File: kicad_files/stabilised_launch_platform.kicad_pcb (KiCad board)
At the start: 2 copper layers, 20 parts, among them J1 Conn_01x03_Male, J2 Conn_01x03_Male, J3 Conn_01x04_Male, SW1 SW_Push, U1 MAX7375AXR805, U2 AP7370-33Y, U3 STM32L011F3Px

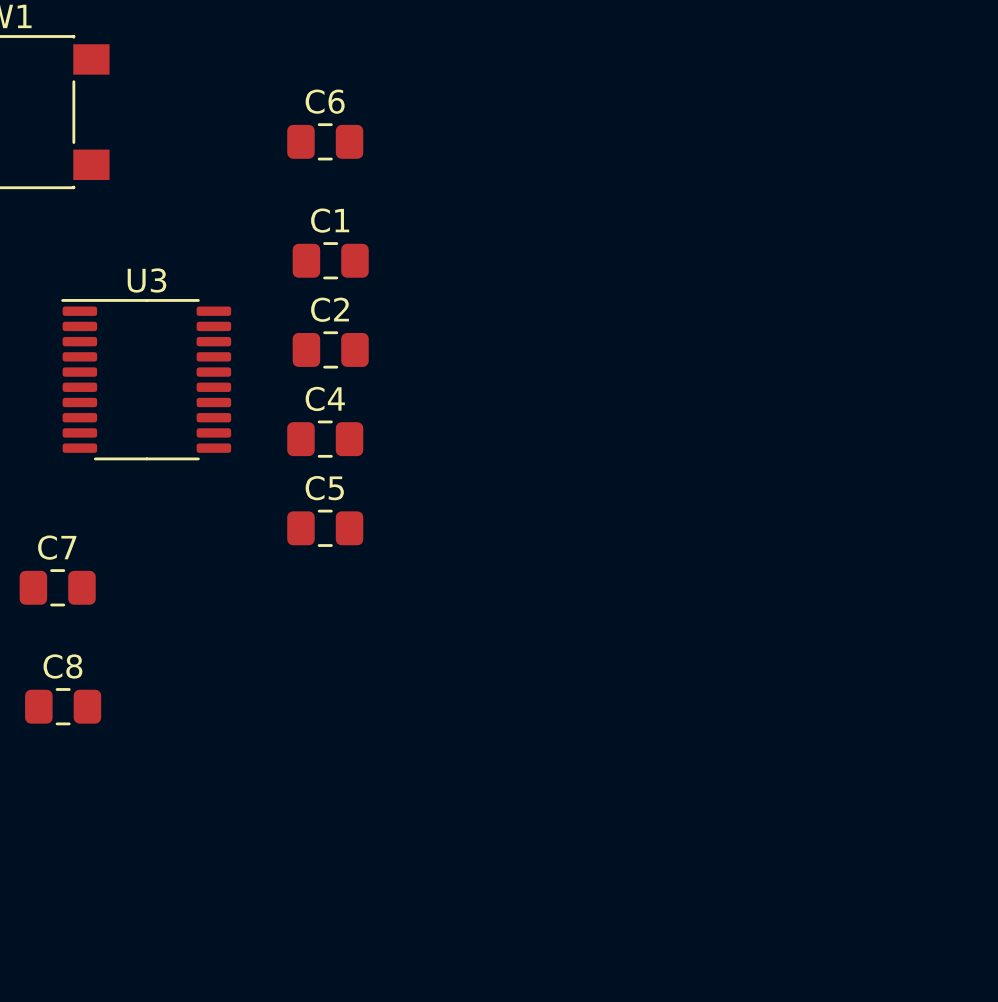
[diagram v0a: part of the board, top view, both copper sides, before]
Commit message: Added accelerometer and MOSFETs to schematic and PCB
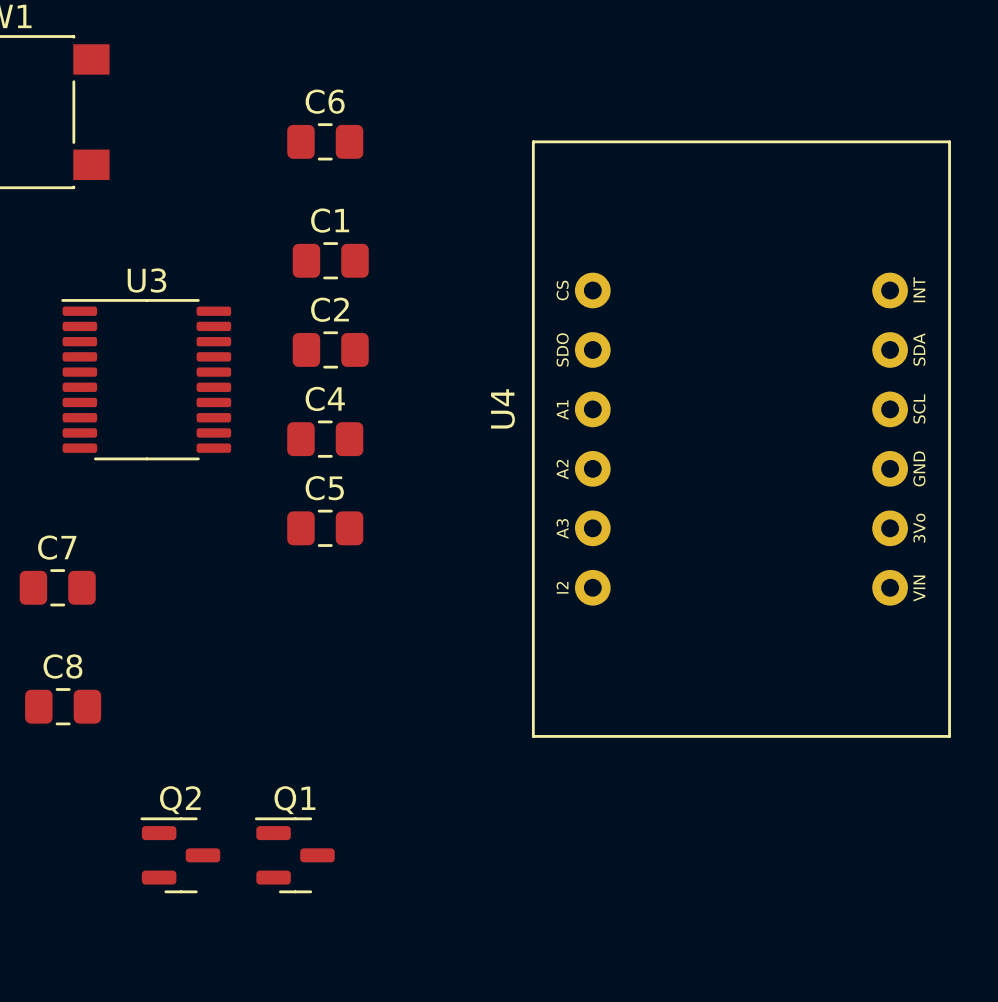
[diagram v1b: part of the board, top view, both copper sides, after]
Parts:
- added Q1: AO3400A, Package_TO_SOT_SMD:SOT-23, F.Cu at (133.3, 101.6)
- added Q2: AO3400A, Package_TO_SOT_SMD:SOT-23, F.Cu at (128.5, 101.6)
- added U4: LIS3DH, CustomFootprints:LIS3DH Accelerometer, F.Cu at (152.4, 83.8)
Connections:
- C7 pad 1: +5V -> SERVO2_SIG_AMP
- J1 pad 1: SERVO1_SIG -> SERVO2_SIG_AMP
- J1 pad 2: +5V -> SERVO2_SIG_AMP
- J2 pad 1: SERVO2_SIG -> SERVO2_SIG_AMP
- J2 pad 2: +5V -> SERVO2_SIG_AMP
- J3 pad 1: +5V -> SERVO2_SIG_AMP
- U2 pad 3: +5V -> SERVO2_SIG_AMP
- U3 pad 11: unconnected-(U3-Pad11) -> POT1
- U3 pad 12: unconnected-(U3-Pad12) -> POT2
- U3 pad 13: POT1 -> POT3
- U3 pad 8: unconnected-(U3-Pad8) -> SERVO1_SIG
- U3 pad 9: unconnected-(U3-Pad9) -> SERVO2_SIG

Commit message: Schematic finished
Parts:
- added C10: 47p, Capacitor_SMD:C_0805_2012Metric_Pad1.18x1.45mm_HandSolder, F.Cu at (110.5, 105.7)
- added C11: 10n, Capacitor_SMD:C_0805_2012Metric_Pad1.18x1.45mm_HandSolder, F.Cu at (105.7, 111.8)
- added C12: 0.1u, Capacitor_SMD:C_0805_2012Metric_Pad1.18x1.45mm_HandSolder, F.Cu at (105.7, 105.7)
- added C13: 47p, Capacitor_SMD:C_0805_2012Metric_Pad1.18x1.45mm_HandSolder, F.Cu at (115.3, 108.8)
- added C14: 4.7u, Capacitor_SMD:C_0805_2012Metric_Pad1.18x1.45mm_HandSolder, F.Cu at (145.6, 80.3)
- added C9: 0.1u, Capacitor_SMD:C_0805_2012Metric_Pad1.18x1.45mm_HandSolder, F.Cu at (105.7, 108.8)
- added FB1: FerriteBead, Inductor_SMD:L_0805_2012Metric_Pad1.05x1.20mm_HandSolder, F.Cu at (125.7, 108.0)
- added J4: USB_C_Receptacle_USB2.0, Connector_USB:USB_C_Receptacle_GCT_USB4085, F.Cu at (83.5, 97.8)
- added JP1: SolderJumper, Jumper:SolderJumper-2_P1.3mm_Open_Pad1.0x1.5mm, F.Cu at (135.9, 97.8)
- added R3: 5.1k, Resistor_SMD:R_0805_2012Metric_Pad1.20x1.40mm_HandSolder, F.Cu at (145.5, 83.3)
- added R4: 5.1k, Resistor_SMD:R_0805_2012Metric_Pad1.20x1.40mm_HandSolder, F.Cu at (120.1, 110.3)
- added R5: 2.2k, Resistor_SMD:R_0805_2012Metric_Pad1.20x1.40mm_HandSolder, F.Cu at (172.0, 64.4)
- added R6: 2.2k, Resistor_SMD:R_0805_2012Metric_Pad1.20x1.40mm_HandSolder, F.Cu at (120.1, 107.4)
- added R7: 4.7k, Resistor_SMD:R_0805_2012Metric_Pad1.20x1.40mm_HandSolder, F.Cu at (130.6, 97.7)
- added R8: 4.7k, Resistor_SMD:R_0805_2012Metric_Pad1.20x1.40mm_HandSolder, F.Cu at (150.3, 80.3)
- added U5: LIS3DH, CustomFootprints:LIS3DH Accelerometer, F.Cu at (156.4, 69.3)
- J3: value Conn_01x04_Male -> Conn_01x06_Male; footprint Connector_PinHeader_1.00mm:PinHeader_1x04_P1.00mm_Vertical -> Connector_PinHeader_1.00mm:PinHeader_1x06_P1.00mm_Vertical
- R1, R2: value 2.2k -> 27R
- U4: value LIS3DH -> FT201XS; footprint CustomFootprints:LIS3DH Accelerometer -> Package_SO:SSOP-16_3.9x4.9mm_P0.635mm
- moved J1 76.1 mm to (82.3, 108.9)
- moved J2 56.7 mm to (100.1, 105.6)
- moved J3 49.5 mm to (113.8, 97.7), turned to 0 degrees
- moved Q1 47.6 mm to (86.4, 109.6)
- moved C5 45.7 mm to (172.1, 61.4)
- moved R2 43.3 mm to (125.8, 100.7), turned to 0 degrees
- moved RV2 43.1 mm to (82.9, 64.2), turned to 0 degrees
- moved C1 43.1 mm to (110.5, 111.8)
- moved R1 40.1 mm to (125.8, 103.6), turned to 0 degrees
- moved SW1 37.9 mm to (97.8, 100.1)
- moved U4 36.5 mm to (119.5, 99.6), turned to 0 degrees
- moved C6 36.3 mm to (120.1, 104.4)
- moved U1 36.2 mm to (150.1, 83.6), turned to 0 degrees
- moved C8 36.1 mm to (91.3, 111.8)
- moved C4 34.0 mm to (115.3, 111.8)
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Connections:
- C7 pad 1: SERVO2_SIG_AMP -> +5V
- J1 pad 1: SERVO2_SIG_AMP -> SERVO1_SIG
- J1 pad 2: SERVO2_SIG_AMP -> +5V
- J2 pad 1: SERVO2_SIG_AMP -> SERVO2_SIG
- J2 pad 2: SERVO2_SIG_AMP -> +5V
- J3 pad 1: SERVO2_SIG_AMP -> +5V
- J3 pad 4: GND -> MCU_TX
- Q1 pad 3: SERVO2_SIG_AMP -> SERVO1_SIG_AMP
- R1 pad 1: +3.3V -> USBDM
- R1 pad 2: SCL -> Net-(R1-Pad2)
- R2 pad 1: +3.3V -> USBDP
- R2 pad 2: SDA -> Net-(R2-Pad2)
- U2 pad 3: SERVO2_SIG_AMP -> +5V
- U3 pad 1: unconnected-(U3-Pad1) -> +3.3V
- U3 pad 10: SCL -> SERVO2_SIG
- U3 pad 17: unconnected-(U3-Pad17) -> SCL
- U3 pad 7: unconnected-(U3-Pad7) -> SERVO1_SIG
- U3 pad 8: SERVO1_SIG -> MCU_TX
- U3 pad 9: SERVO2_SIG -> MCU_RX
- U4 pad 10: GND -> FTDI_3V3
- U4 pad 11: unconnected-(U4-Pad11) -> FTDI_3V3
- U4 pad 12: GND -> Net-(JP1-Pad2)
- U4 pad 2: unconnected-(U4-Pad2) -> SCL
- U4 pad 3: unconnected-(U4-Pad3) -> FTDI_3V3
- U4 pad 4: SCL -> SDA
- U4 pad 6: SDA -> unconnected-(U4-Pad6)
- U4 pad 8: unconnected-(U4-Pad8) -> Net-(R2-Pad2)
- U4 pad 9: unconnected-(U4-Pad9) -> Net-(R1-Pad2)

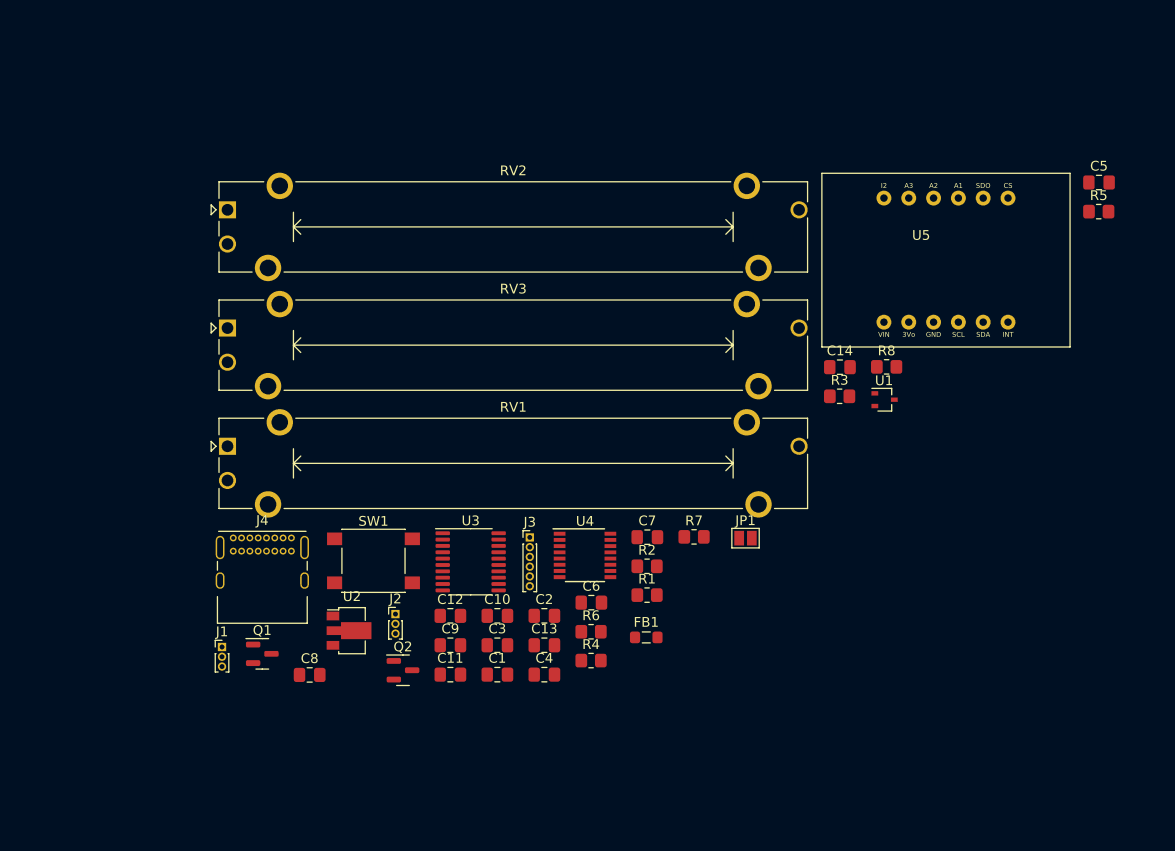
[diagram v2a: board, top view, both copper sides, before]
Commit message: Removed unnecessary mosfets, schematic finished
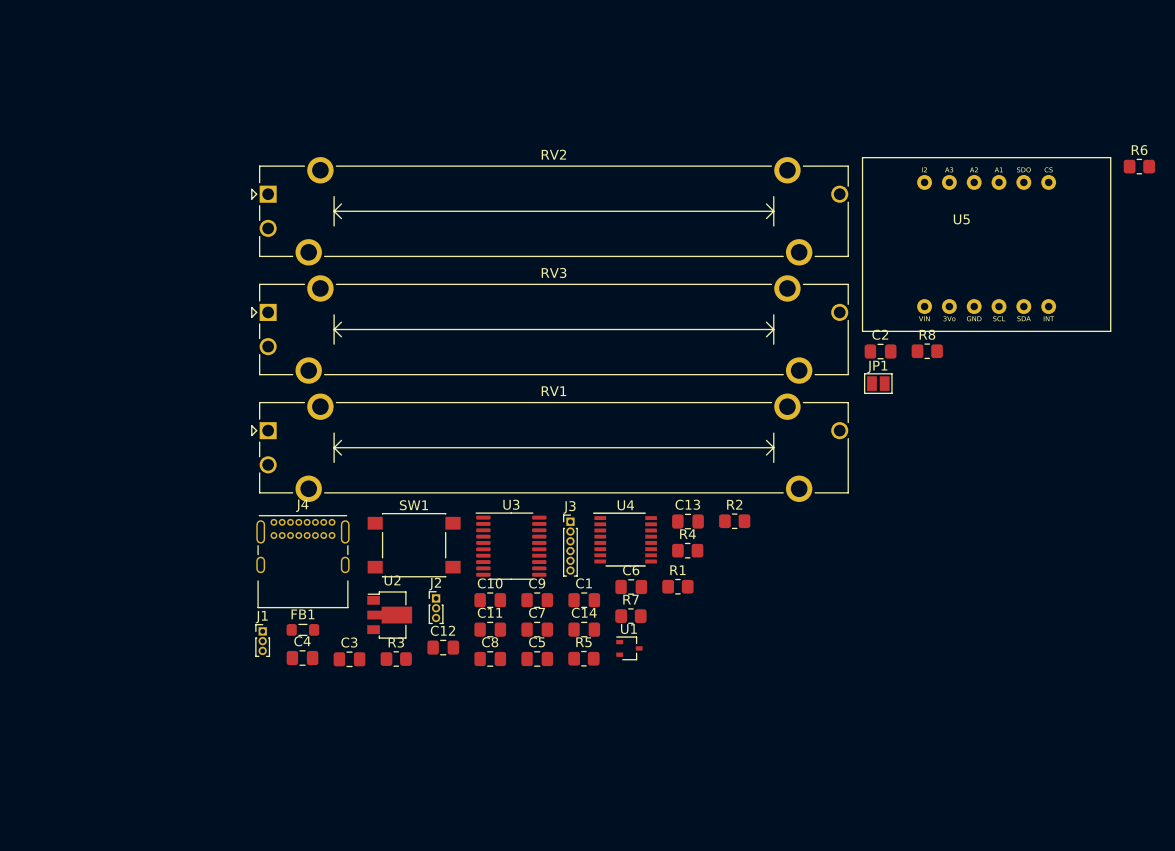
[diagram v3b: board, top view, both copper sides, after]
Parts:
- removed Q1, Q2: AO3400A, Package_TO_SOT_SMD:SOT-23
- moved C5 75.4 mm to (114.6, 110.2)
- moved R6 73.6 mm to (176.2, 59.8)
- moved R5 69.8 mm to (119.3, 110.1)
- moved R3 52.7 mm to (100.1, 110.2)
- moved C2 43.8 mm to (149.7, 78.7)
- moved C14 37.5 mm to (119.4, 107.2)
- moved U1 36.5 mm to (124.0, 109.1)
- moved FB1 35.1 mm to (90.6, 107.2)
- moved C4 24.8 mm to (90.5, 110.1)
- moved JP1 20.9 mm to (149.5, 82.0)
- moved C13 19.4 mm to (130.0, 96.1)
- moved C8 18.6 mm to (109.8, 110.2)
- moved C3 15.2 mm to (95.4, 110.2)
- moved R4 15.0 mm to (130.0, 99.1)
- moved C7 14.7 mm to (114.6, 107.2)
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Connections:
- R7 pad 2: SERVO1_SIG_AMP -> SERVO1_SIG
- R8 pad 2: SERVO2_SIG_AMP -> SERVO2_SIG

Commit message: PCB tracks routed have all components connected, needs a bit of tidying up
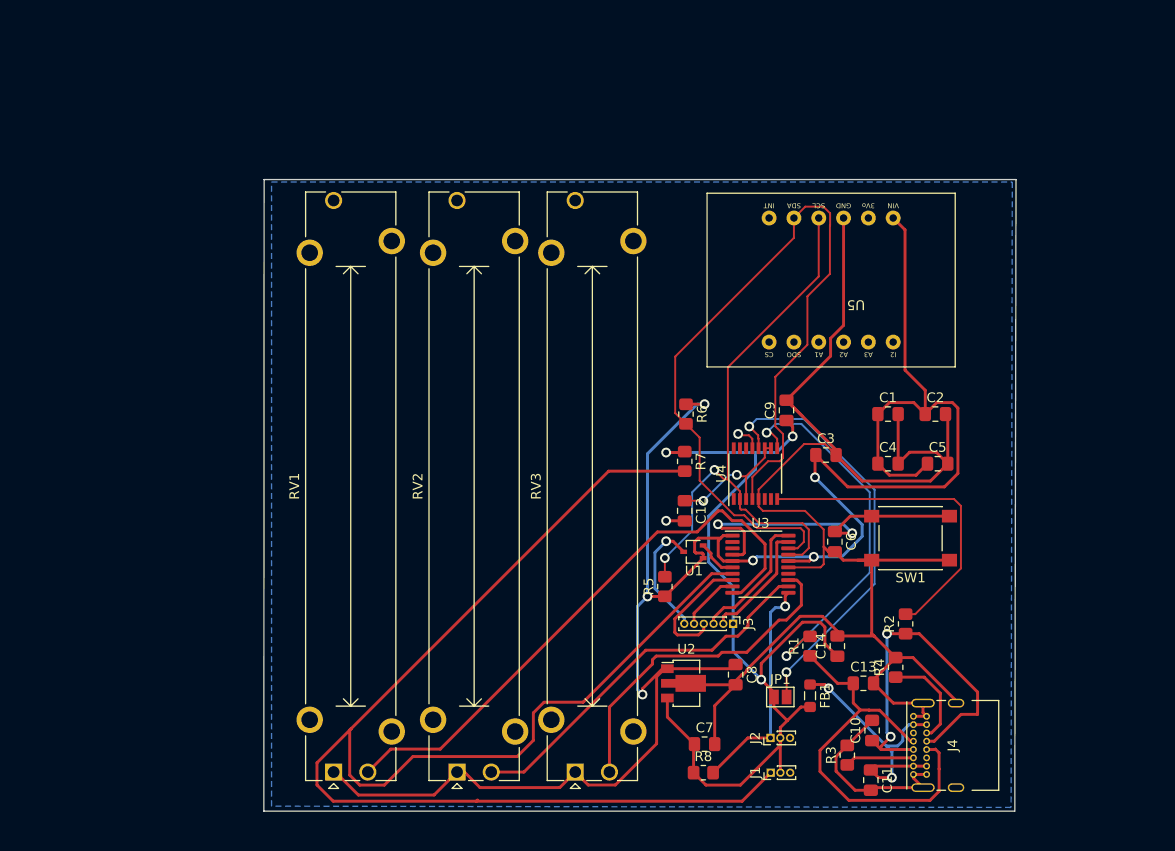
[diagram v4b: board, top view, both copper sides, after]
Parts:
- moved J4 70.4 mm to (153.1, 122.0), turned to 90 degrees
- moved C4 63.1 mm to (150.5, 90.2)
- moved RV2 62.2 mm to (106.4, 121.7), turned to 90 degrees
- moved RV3 56.6 mm to (118.5, 121.7), turned to 90 degrees
- moved J1 54.0 mm to (138.5, 121.8), turned to 90 degrees
- moved C3 53.1 mm to (144.1, 89.3)
- moved R6 52.9 mm to (129.8, 85.1), turned to -90 degrees
- moved FB1 52.3 mm to (142.5, 113.9), turned to -90 degrees
- moved SW1 50.8 mm to (152.8, 97.8), turned to 180 degrees
- moved R8 48.8 mm to (131.6, 121.8)
- moved R3 47.2 mm to (146.3, 120.0), turned to 90 degrees
- moved C5 45.6 mm to (155.6, 90.2)
- moved C11 41.9 mm to (148.7, 122.6), turned to -90 degrees
- moved C10 41.3 mm to (148.8, 117.5), turned to 90 degrees
- moved J2 37.1 mm to (138.4, 118.2), turned to 90 degrees
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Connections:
- U3 pad 10: SERVO2_SIG -> POT1
- U3 pad 11: POT1 -> SERVO2_SIG
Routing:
- net +3.3V: track 0.00 -> 203.7 mm, vias 0 -> 6
- net GND: track 0.00 -> 203.2 mm, vias 0 -> 3
- net SERVO1_SIG: track 0.00 -> 155.8 mm
- net +5V: track 0.00 -> 93.8 mm, vias 0 -> 3
- net SDA: track 0.00 -> 87.0 mm
- net SCL: track 0.00 -> 61.1 mm, vias 0 -> 2
- net POT1: track 0.00 -> 60.0 mm
- net Net-(JP1-Pad2): track 0.00 -> 43.7 mm, vias 0 -> 2
- net USBDM: track 0.00 -> 42.6 mm
- net Net-(R1-Pad2): track 0.00 -> 39.7 mm, vias 0 -> 2
- net POT2: track 0.00 -> 38.8 mm
- net USBDP: track 0.00 -> 37.4 mm, vias 0 -> 2
- net Net-(C6-Pad1): track 0.00 -> 34.8 mm, vias 0 -> 2
- net POT3: track 0.00 -> 34.5 mm
- net Net-(R2-Pad2): track 0.00 -> 33.1 mm
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- added copper zone on B.Cu, net GND
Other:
- board outline added: 77 x 64.6 mm

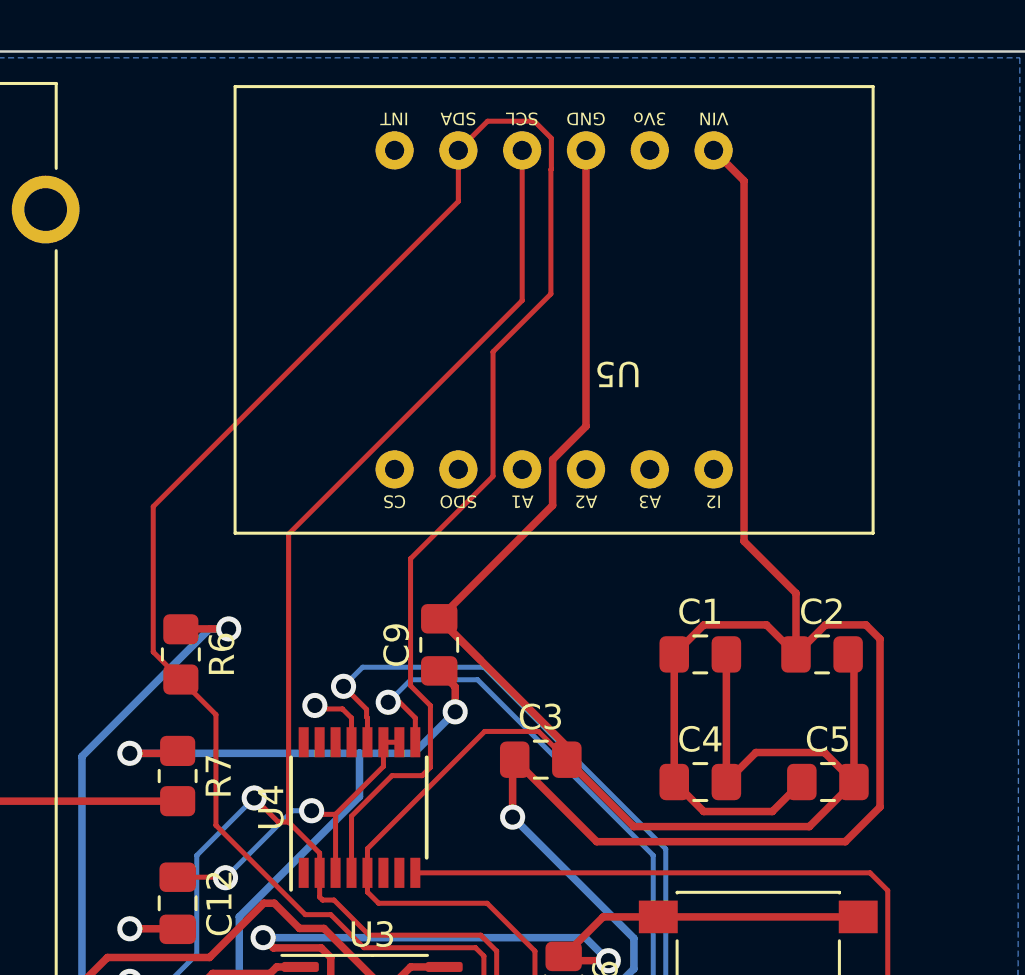
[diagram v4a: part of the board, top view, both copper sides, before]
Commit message: PCB rearrangments
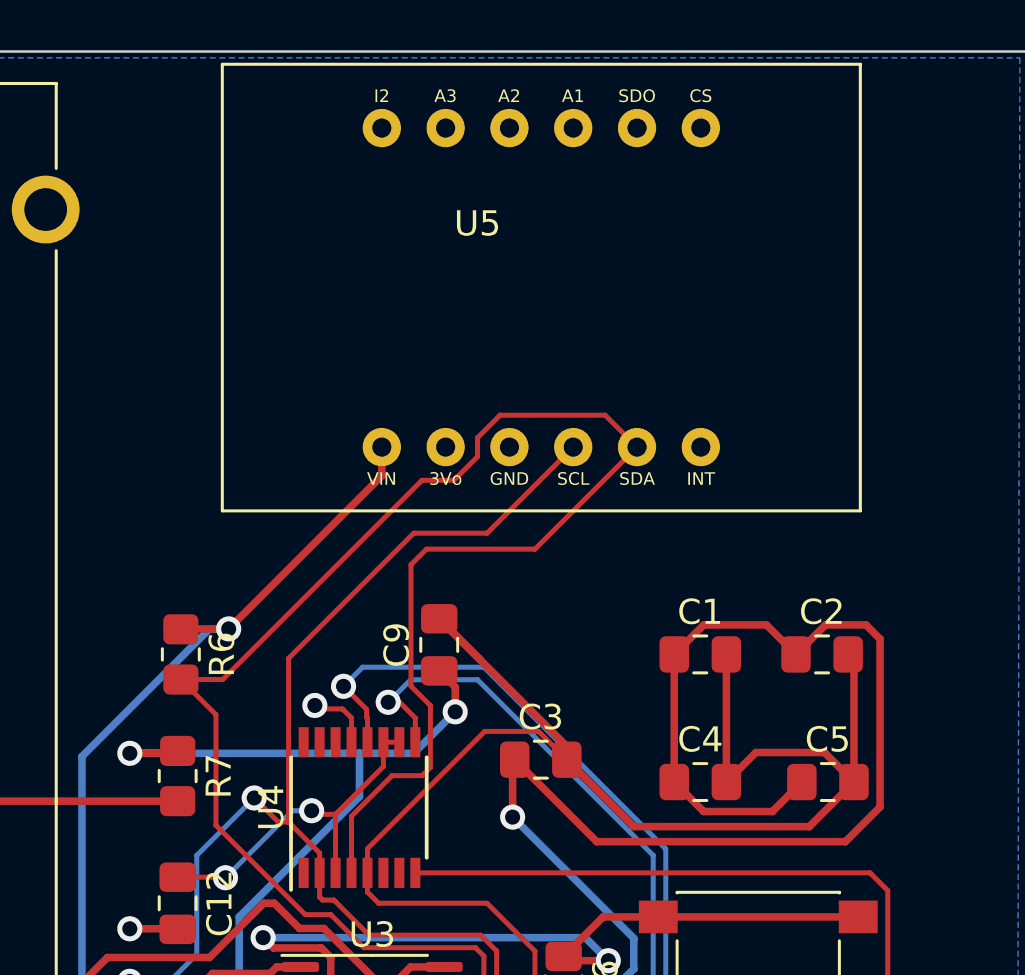
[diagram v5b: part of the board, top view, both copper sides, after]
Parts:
- moved U5 1.02 mm to (144.1, 70.5), turned to 0 degrees
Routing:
- net GND: track 203.2 -> 182.1 mm
- net SDA: track 87.0 -> 71.2 mm
- net +3.3V: track 203.7 -> 192.0 mm
- net SCL: track 61.1 -> 51.9 mm
